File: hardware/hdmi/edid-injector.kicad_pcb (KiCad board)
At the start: 2 copper layers, 35.3 x 62.5 mm, 44 parts, among them SW1 SW_PUSH, U1 C8051F381/3/5/7/C-GQ

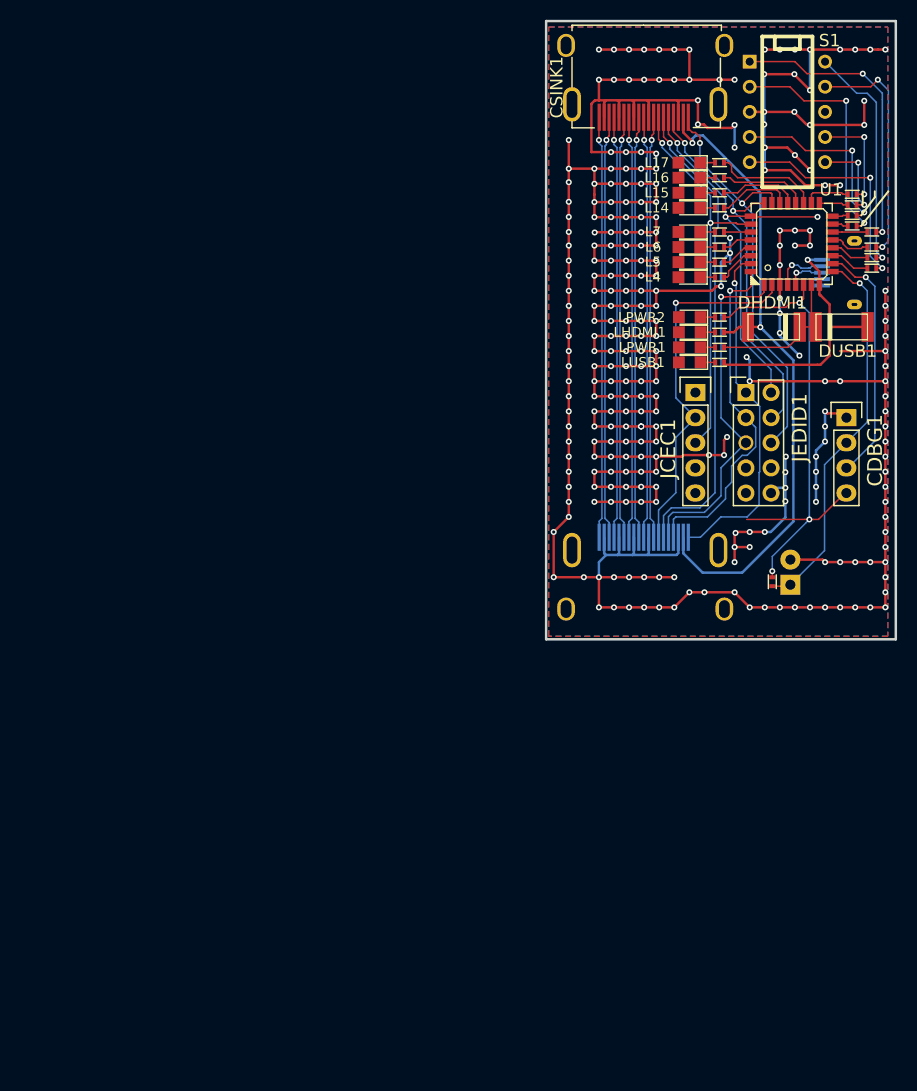
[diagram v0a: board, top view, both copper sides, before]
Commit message: Version 1.0 of simple edid eeprom
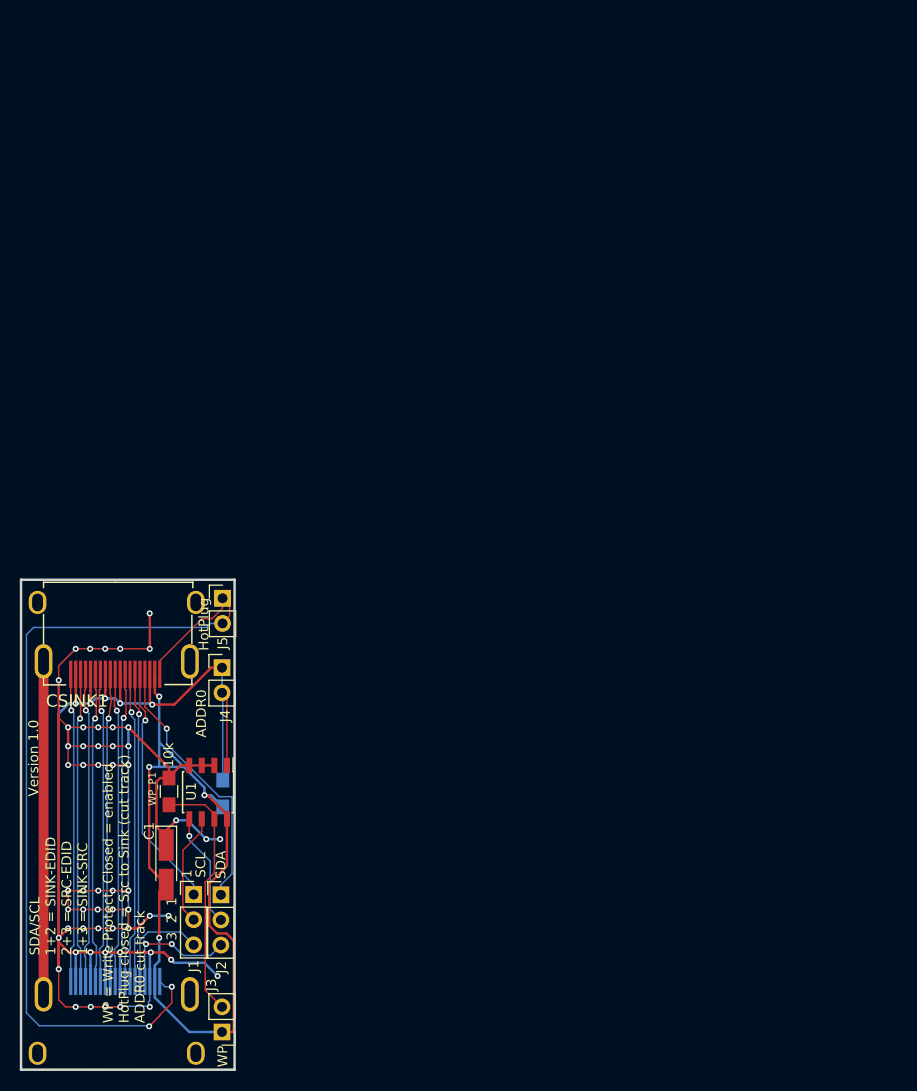
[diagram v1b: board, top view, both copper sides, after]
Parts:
- removed CDBG1: CONN_01X04, Pin_Headers:Pin_Header_Straight_1x04
- removed CUSB1: USB-MINI-B2, micro-usb:micro-usb
- removed DHDMI1, DUSB1: DIODE, sod323:sod323
- removed JCEC1: CONN_01X05, Pin_Headers:Pin_Header_Straight_1x05
- removed JEDID1: CONN_02X05, Pin_Headers:Pin_Header_Straight_2x05
- removed L14, L15, L16, L17, L4, L5, L6, L7, LHDMI1, LPWR1, LPWR2, LUSB1: LED, LEDs:LED_0805
- removed RHDMI1, RL14, RL15, RL16, RL17, RL4, RL5, RL6, RL7, RPWR1, RPWR2, RRST1, RSEGA1, RSEGB1, RSEGC1, RSEGD1, RSEGE1, RSEGF1, RSEGG1, RSEGP1, RUSB1: R, random:R_0402
- removed S1: 7SEGM, Sockets_DIP:DIP-10__300
- removed SW1: SW_PUSH, Pin_Headers:Pin_Header_Angled_1x02
- added ADDR0_P1: 10k, Resistors_SMD:R_0805_HandSoldering, B.Cu at (61.2, 137.8)
- added C1: C_PWR, Capacitors_Tantalum_SMD:CP_Tantalum_Case-A_EIA-3216-18_Hand, F.Cu at (55.4, 145.0)
- added J1: SCL, Pin_Headers:Pin_Header_Straight_1x03_Pitch2.54mm, F.Cu at (58.2, 148.0)
- added J2: SDA, Pin_Headers:Pin_Header_Straight_1x03_Pitch2.54mm, F.Cu at (61.0, 148.0)
- added J3: WP, Pin_Headers:Pin_Header_Straight_1x02_Pitch2.54mm, F.Cu at (61.1, 161.9)
- added J4: ADDR0, Pin_Headers:Pin_Header_Straight_1x02_Pitch2.54mm, F.Cu at (61.1, 125.1)
- added J5: HotPlug, Pin_Headers:Pin_Header_Straight_1x02_Pitch2.54mm, F.Cu at (61.1, 118.1)
- added WP_P1: 10k, Resistors_SMD:R_0805_HandSoldering, F.Cu at (55.7, 137.6)
- U1: value C8051F381/3/5/7/C-GQ -> 24LC16; footprint QFP:lqfp32 -> Housings_SOIC:SOIC-8_3.9x4.9mm_Pitch1.27mm
- moved U1 80.9 mm to (59.7, 137.7), turned to 270 degrees
- moved CSINK1 77.6 mm to (50.3, 124.4)
- moved CSRC1 69.8 mm to (50.3, 158.1)
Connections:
- CSRC1 pad 13: /SRC_CEC -> /SINK_CEC
- U1 pad 1: /SRC_SCL -> Net-(ADDR0_P1-Pad1)
- U1 pad 2: /SRC_CEC -> GND
- U1 pad 4: /D+ -> GND
- U1 pad 5: /D- -> Net-(J2-Pad2)
- U1 pad 6: /VCC3V3 -> Net-(J1-Pad2)
- U1 pad 7: /VCC5V0 -> Net-(J3-Pad2)
- U1 pad 8: /VUSB -> /VHDMI
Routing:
- net GND: track 537.8 -> 255.8 mm, vias 269 -> 61
- net /VCC3V3: track 69.4 -> 0.00 mm, vias 13 -> 0
- net /SRC_HPD: track 35.2 -> 80.1 mm, vias 1 -> 2
- net Net-(CDBG1-Pad2): track 39.2 -> 0.00 mm, vias 1 -> 0
- net /SRC_CEC: track 37.1 -> 0.00 mm, vias 1 -> 0
- net (no net): track 0.00 -> 33.7 mm
- net /SINK_HPD: track 42.4 -> 9.54 mm, vias 2 -> 0
- net Net-(RSEGE1-Pad2): track 29.4 -> 0.00 mm, vias 2 -> 0
- net /VUSB: track 27.0 -> 0.00 mm, vias 1 -> 0
- net /SRC_SCL: track 36.1 -> 10.5 mm, vias 1 -> 0
- net Net-(J3-Pad2): track 0.00 -> 25.5 mm
- net Net-(CDBG1-Pad3): track 24.9 -> 0.00 mm, vias 1 -> 0
- net Net-(RSEGD1-Pad2): track 24.3 -> 0.00 mm, vias 2 -> 0
- net Net-(RSEGF1-Pad2): track 23.9 -> 0.00 mm, vias 2 -> 0
- net Net-(RSEGG1-Pad2): track 23.5 -> 0.00 mm, vias 1 -> 0
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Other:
- board size 35.3 x 62.5 mm -> 21.6 x 49.5 mm
- board text added: "1"
- board text added: "3 2 1"
- board text added: "SDA/SCL 1+2 = SINK-EDID 2+3 = SRC-EDID 1+3 = SINK-SRC"
- board text added: "Version 1.0"
- board text added: "WP = Write Protect. Closed = enabled HotPlug closed = Src to Sink (cut track) ADDR0 cut track"
- board text removed: "35.35 mm"
- board text removed: "62.50 mm"
